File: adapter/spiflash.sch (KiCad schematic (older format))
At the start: 45 parts, among them J1 USB_C_Receptacle_USB2.0, J2 Tag-Connect, J3 Conn_01x02, J4 Conn_01x03, J5 Clip, U1 XC6206, U2 SRV05-4-P-T7, U4 STM32F103C8T6, U5 SN74LVC1T45DBV, U6 SN74LVC1T45DBV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

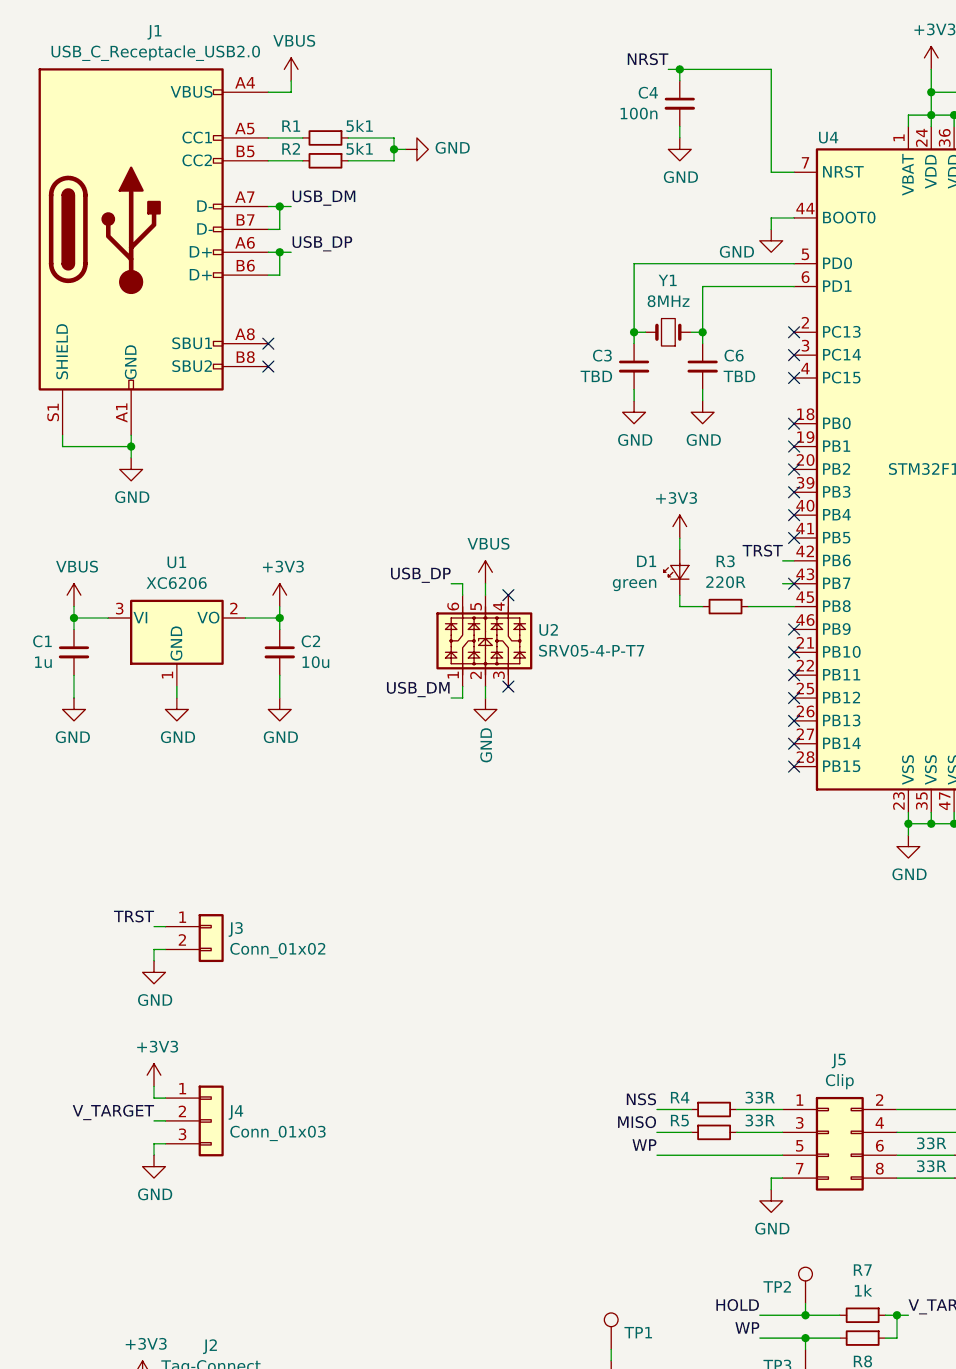
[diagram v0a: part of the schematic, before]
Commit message: adapter: make ERC happy
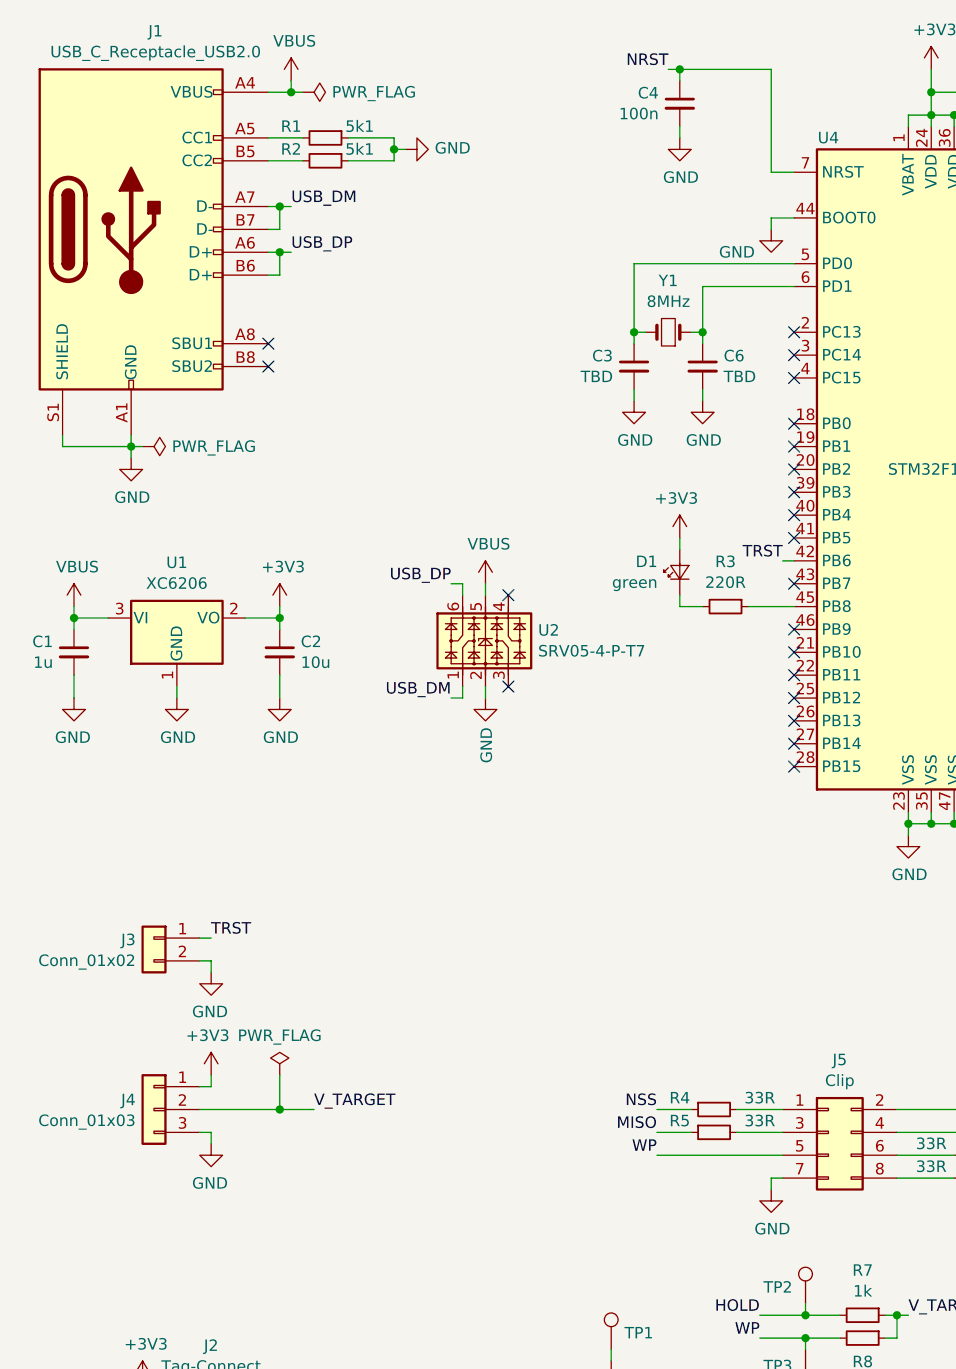
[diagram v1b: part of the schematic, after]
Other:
- moved on the sheet: J3, J4
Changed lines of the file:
@@
 L Connector_Generic:Conn_01x03 J4
 U 1 1 5D77DCB7
-P 1350 5500
-F 0 "J4" H 1430 5542 50  0000 L CNN
-F 1 "Conn_01x03" H 1430 5451 50  0000 L CNN
-F 2 "Connector_PinHeader_2.54mm:PinHeader_1x03_P2.54mm_Vertical" H 1350 5500 50  0001 C CNN
-F 3 "~" H 1350 5500 50  0001 C CNN
-	1    1350 5500
-	1    0    0    -1
+P 1100 5450
+F 0 "J4" H 1180 5492 50  0000 L CNN
+F 1 "Conn_01x03" H 1180 5401 50  0000 L CNN
+F 2 "Connector_PinHeader_2.54mm:PinHeader_1x03_P2.54mm_Vertical" H 1100 5450 50  0001 C CNN
+F 3 "~" H 1100 5450 50  0001 C CNN
+	1    1100 5450
+	-1   0    0    -1
 $EndComp
 $Comp
 L power:+3V3 #PWR07
 U 1 1 5D77E294
-P 1100 5350
-F 0 "#PWR07" H 1100 5200 50  0001 C CNN
-F 1 "+3V3" H 1115 5523 50  0000 C CNN
-F 2 "" H 1100 5350 50  0001 C CNN
-F 3 "" H 1100 5350 50  0001 C CNN
-	1    1100 5350
-	1    0    0    -1
-$EndComp
-Wire Wire Line
-	1100 5350 1100 5400
-Wire Wire Line
-	1100 5400 1150 5400
-Text Label 1100 5500 2    50   ~ 0
+P 1350 5300
+F 0 "#PWR07" H 1350 5150 50  0001 C CNN
+F 1 "+3V3" H 1365 5473 50  0000 C CNN
+F 2 "" H 1350 5300 50  0001 C CNN
+F 3 "" H 1350 5300 50  0001 C CNN
+	1    1350 5300
+	-1   0    0    -1
+$EndComp
+Wire Wire Line
+	1350 5300 1350 5350
+Wire Wire Line
+	1350 5350 1300 5350
+Text Label 1800 5450 0    50   ~ 0
 V_TARGET
 Wire Wire Line
-	1100 5500 1150 5500
+	1800 5450 1650 5450
 $Comp
 L power:GND #PWR08
 U 1 1 5D7828DE
-P 1100 5650
-F 0 "#PWR08" H 1100 5400 50  0001 C CNN
-F 1 "GND" H 1105 5477 50  0000 C CNN
-F 2 "" H 1100 5650 50  0001 C CNN
-F 3 "" H 1100 5650 50  0001 C CNN
-	1    1100 5650
-	1    0    0    -1
-$EndComp
-Wire Wire Line
-	1100 5650 1100 5600
-Wire Wire Line
-	1100 5600 1150 5600
+P 1350 5600
+F 0 "#PWR08" H 1350 5350 50  0001 C CNN
+F 1 "GND" H 1355 5427 50  0000 C CNN
+F 2 "" H 1350 5600 50  0001 C CNN
+F 3 "" H 1350 5600 50  0001 C CNN
+	1    1350 5600
+	-1   0    0    -1
+$EndComp
+Wire Wire Line
+	1350 5600 1350 5550
+Wire Wire Line
+	1350 5550 1300 5550
 Wire Wire Line
 	4500 900  4500 1000
@@
 L Connector_Generic:Conn_01x02 J3
 U 1 1 5DA10A5A
-P 1350 4650
-F 0 "J3" H 1430 4642 50  0000 L CNN
-F 1 "Conn_01x02" H 1430 4551 50  0000 L CNN
-F 2 "Connector_PinHeader_2.54mm:PinHeader_1x02_P2.54mm_Vertical" H 1350 4650 50  0001 C CNN
-F 3 "~" H 1350 4650 50  0001 C CNN
-	1    1350 4650
-	1    0    0    -1
+P 1100 4700
+F 0 "J3" H 1180 4692 50  0000 L CNN
+F 1 "Conn_01x02" H 1180 4601 50  0000 L CNN
+F 2 "Connector_PinHeader_2.54mm:PinHeader_1x02_P2.54mm_Vertical" H 1100 4700 50  0001 C CNN
+F 3 "~" H 1100 4700 50  0001 C CNN
+	1    1100 4700
+	-1   0    0    -1
 $EndComp
 $Comp
 L power:GND #PWR06
 U 1 1 5DA10DAA
-P 1100 4800
-F 0 "#PWR06" H 1100 4550 50  0001 C CNN
-F 1 "GND" H 1105 4627 50  0000 C CNN
-F 2 "" H 1100 4800 50  0001 C CNN
-F 3 "" H 1100 4800 50  0001 C CNN
-	1    1100 4800
-	1    0    0    -1
-$EndComp
-Wire Wire Line
-	1150 4750 1100 4750
-Wire Wire Line
-	1100 4750 1100 4800
-Text Label 1100 4650 2    50   ~ 0
+P 1350 4850
+F 0 "#PWR06" H 1350 4600 50  0001 C CNN
+F 1 "GND" H 1355 4677 50  0000 C CNN
+F 2 "" H 1350 4850 50  0001 C CNN
+F 3 "" H 1350 4850 50  0001 C CNN
+	1    1350 4850
+	-1   0    0    -1
+$EndComp
+Wire Wire Line
+	1300 4800 1350 4800
+Wire Wire Line
+	1350 4800 1350 4850
+Text Label 1350 4700 0    50   ~ 0
 TRST
 Wire Wire Line
-	1100 4650 1150 4650
+	1350 4700 1300 4700
 Text Label 2400 3150 2    50   ~ 0
 USB_DP
@@
 Text Label 3850 3050 2    50   ~ 0
 TRST
-Wire Wire Line
-	3900 3150 3850 3150
 $Comp
 L Power_Protection:NUP4202 U2
@@
 Wire Wire Line
 	3900 3050 3850 3050
+$Comp
+L power:PWR_FLAG #FLG0101
+U 1 1 5D8AAFC9
+P 1050 2550
+F 0 "#FLG0101" H 1050 2625 50  0001 C CNN
+F 1 "PWR_FLAG" V 1050 2678 50  0000 L CNN
+F 2 "" H 1050 2550 50  0001 C CNN
+F 3 "~" H 1050 2550 50  0001 C CNN
+	1    1050 2550
+	0    1    1    0
+$EndComp
+Wire Wire Line
+	1050 2550 1000 2550
+$Comp
+L power:PWR_FLAG #FLG0102
+U 1 1 5D8B979E
+P 1750 1000
+F 0 "#FLG0102" H 1750 1075 50  0001 C CNN
+F 1 "PWR_FLAG" V 1750 1128 50  0000 L CNN
+F 2 "" H 1750 1000 50  0001 C CNN
+F 3 "~" H 1750 1000 50  0001 C CNN
+	1    1750 1000
+	0    1    1    0
+$EndComp
+Wire Wire Line
+	1750 1000 1700 1000
+Connection ~ 1700 1000
+$Comp
+L power:PWR_FLAG #FLG0103
+U 1 1 5D8C7F3E
+P 1650 5300
+F 0 "#FLG0103" H 1650 5375 50  0001 C CNN
+F 1 "PWR_FLAG" H 1650 5473 50  0000 C CNN
+F 2 "" H 1650 5300 50  0001 C CNN
+F 3 "~" H 1650 5300 50  0001 C CNN
+	1    1650 5300
+	-1   0    0    -1
+$EndComp
+Wire Wire Line
+	1650 5300 1650 5450
+Connection ~ 1650 5450
+Wire Wire Line
+	1650 5450 1300 5450
 $EndSCHEMATC

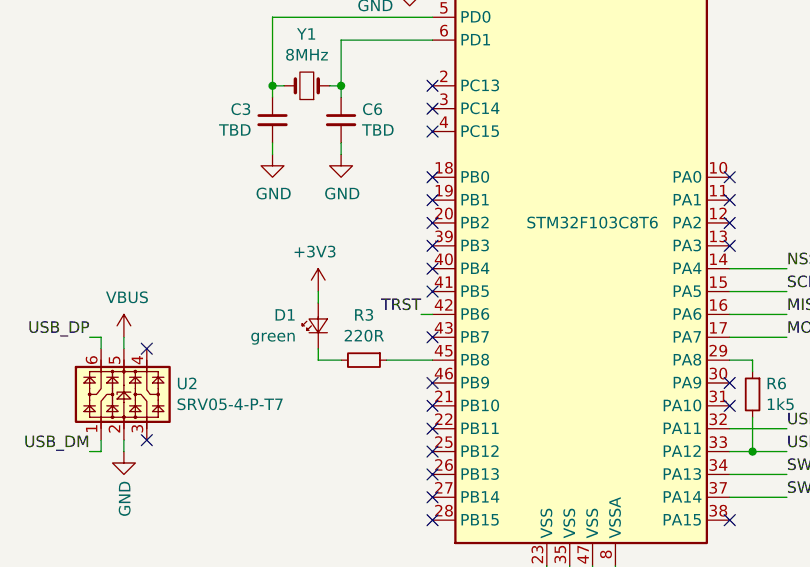
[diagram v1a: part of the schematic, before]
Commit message: remap TRST
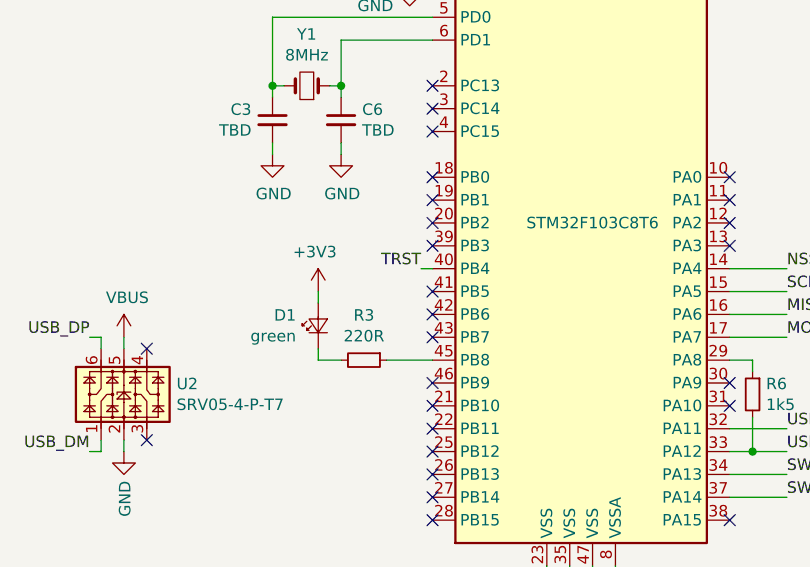
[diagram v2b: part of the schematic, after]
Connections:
- net TRST: now also U4.40 (PB4); no longer U4.42 (PB6)
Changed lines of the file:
@@
 Wire Wire Line
 	1650 6700 1600 6700
-NoConn ~ 1600 6900
 Wire Wire Line
 	4500 1100 4400 1100
@@
 NoConn ~ 3900 2550
 NoConn ~ 3900 2650
-NoConn ~ 3900 2750
-NoConn ~ 3900 2850
 NoConn ~ 3900 2950
 NoConn ~ 3900 3150
@@
 Text Label 2400 3650 2    50   ~ 0
 USB_DM
-Text Label 3850 3050 2    50   ~ 0
+Text Label 3850 2850 2    50   ~ 0
 TRST
 $Comp
@@
 NoConn ~ 2650 3600
 Wire Wire Line
-	3900 3050 3850 3050
+	3900 2850 3850 2850
 $Comp
 L power:PWR_FLAG #FLG0101
@@
 Wire Wire Line
 	1650 5450 1300 5450
+NoConn ~ 3900 3050
+NoConn ~ 1600 6900
+NoConn ~ 3900 2750
 $EndSCHEMATC

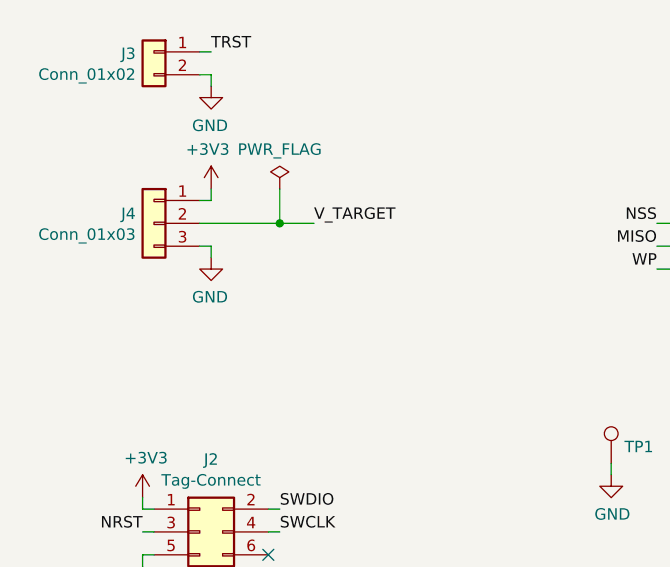
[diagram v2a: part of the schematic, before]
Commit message: adapter: add Vtarget decoupling
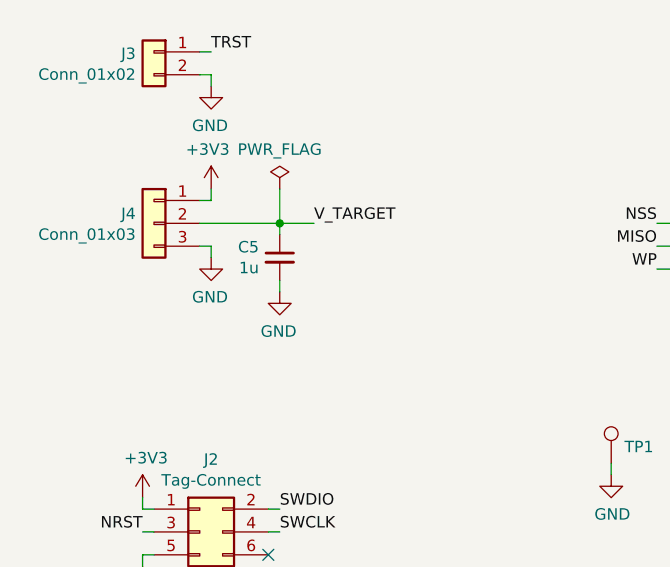
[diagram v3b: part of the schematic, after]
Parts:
- added C5: 1u, Capacitor_SMD:C_0603_1608Metric, symbol Device:C_Small
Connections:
- net GND: now also C5.2
- net V_TARGET: now also C5.1
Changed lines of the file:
@@
 Wire Wire Line
 	1800 5450 1650 5450
-$Comp
-L power:GND #PWR08
-U 1 1 5D7828DE
-P 1350 5600
-F 0 "#PWR08" H 1350 5350 50  0001 C CNN
-F 1 "GND" H 1355 5427 50  0000 C CNN
-F 2 "" H 1350 5600 50  0001 C CNN
-F 3 "" H 1350 5600 50  0001 C CNN
-	1    1350 5600
-	-1   0    0    -1
-$EndComp
-Wire Wire Line
-	1350 5600 1350 5550
 Wire Wire Line
 	1350 5550 1300 5550
@@
 NoConn ~ 1600 6900
 NoConn ~ 3900 2750
+$Comp
+L Device:C_Small C5
+U 1 1 5D89EB58
+P 1650 5600
+F 0 "C5" H 1741 5646 50  0000 L CNN
+F 1 "1u" H 1741 5555 50  0000 L CNN
+F 2 "Capacitor_SMD:C_0603_1608Metric" H 1650 5600 50  0001 C CNN
+F 3 "~" H 1650 5600 50  0001 C CNN
+F 4 "C15849" H 1650 5600 50  0001 C CNN "LCSC"
+F 5 "CL10A105KB8NNNC" H 1650 5600 50  0001 C CNN "MPN"
+F 6 "Samsung Electro-Mechanics" H 1650 5600 50  0001 C CNN "Manufacturer"
+	1    1650 5600
+	-1   0    0    -1
+$EndComp
+Wire Wire Line
+	1350 5600 1350 5550
+$Comp
+L power:GND #PWR08
+U 1 1 5D7828DE
+P 1350 5600
+F 0 "#PWR08" H 1350 5350 50  0001 C CNN
+F 1 "GND" H 1355 5427 50  0000 C CNN
+F 2 "" H 1350 5600 50  0001 C CNN
+F 3 "" H 1350 5600 50  0001 C CNN
+	1    1350 5600
+	-1   0    0    -1
+$EndComp
+$Comp
+L power:GND #PWR017
+U 1 1 5D8ADED4
+P 1650 5750
+F 0 "#PWR017" H 1650 5500 50  0001 C CNN
+F 1 "GND" H 1655 5577 50  0000 C CNN
+F 2 "" H 1650 5750 50  0001 C CNN
+F 3 "" H 1650 5750 50  0001 C CNN
+	1    1650 5750
+	-1   0    0    -1
+$EndComp
+Wire Wire Line
+	1650 5500 1650 5450
+Wire Wire Line
+	1650 5750 1650 5700
 $EndSCHEMATC

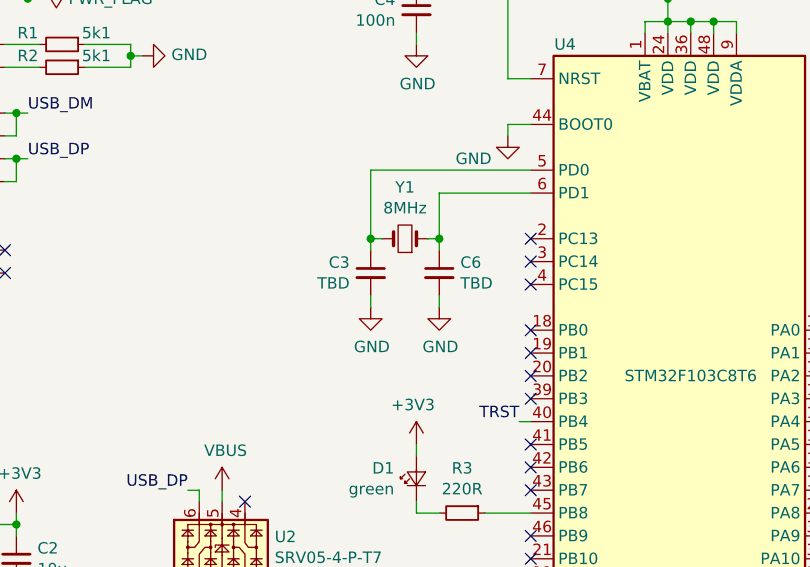
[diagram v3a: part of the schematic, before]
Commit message: adapter: define crystal loading caps, reexport fab
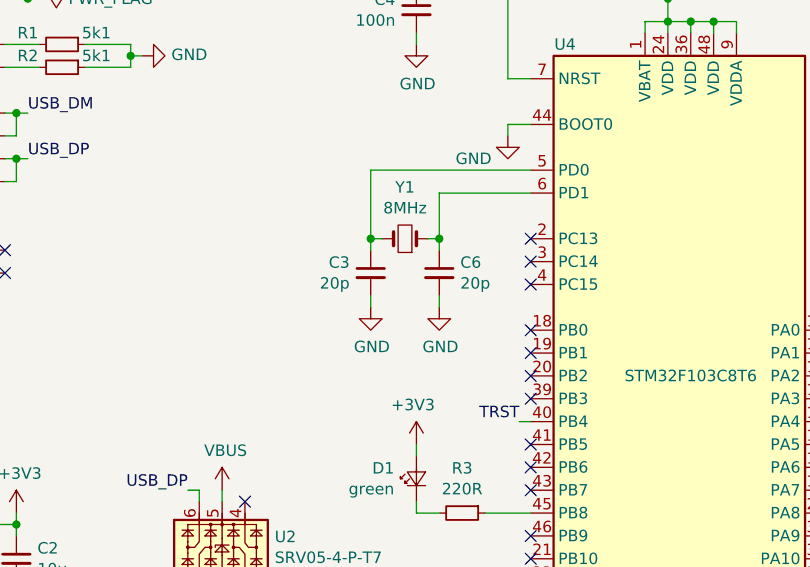
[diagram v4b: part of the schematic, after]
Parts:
- C3, C6: value TBD -> 20p; LCSC (none) -> C1554; MPN (none) -> 0402CG200J500NT; Manufacturer (none) -> Guangdong Fenghua Advanced Tech
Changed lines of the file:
@@
 P 3200 2200
 F 0 "C3" H 3108 2246 50  0000 R CNN
-F 1 "TBD" H 3108 2155 50  0000 R CNN
+F 1 "20p" H 3108 2155 50  0000 R CNN
 F 2 "Capacitor_SMD:C_0402_1005Metric" H 3200 2200 50  0001 C CNN
 F 3 "~" H 3200 2200 50  0001 C CNN
+F 4 "C1554" H 3200 2200 50  0001 C CNN "LCSC"
+F 5 "0402CG200J500NT" H 3200 2200 50  0001 C CNN "MPN"
+F 6 "Guangdong Fenghua Advanced Tech" H 3200 2200 50  0001 C CNN "Manufacturer"
 	1    3200 2200
 	1    0    0    -1
@@
 P 3500 2200
 F 0 "C6" H 3592 2246 50  0000 L CNN
-F 1 "TBD" H 3592 2155 50  0000 L CNN
+F 1 "20p" H 3592 2155 50  0000 L CNN
 F 2 "Capacitor_SMD:C_0402_1005Metric" H 3500 2200 50  0001 C CNN
 F 3 "~" H 3500 2200 50  0001 C CNN
+F 4 "C1554" H 3500 2200 50  0001 C CNN "LCSC"
+F 5 "0402CG200J500NT" H 3500 2200 50  0001 C CNN "MPN"
+F 6 "Guangdong Fenghua Advanced Tech" H 3500 2200 50  0001 C CNN "Manufacturer"
 	1    3500 2200
 	1    0    0    -1
